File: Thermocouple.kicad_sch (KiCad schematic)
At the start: 9 parts, among them J7 K-TYPE THERMOCOUPLE, U7 MAX31856

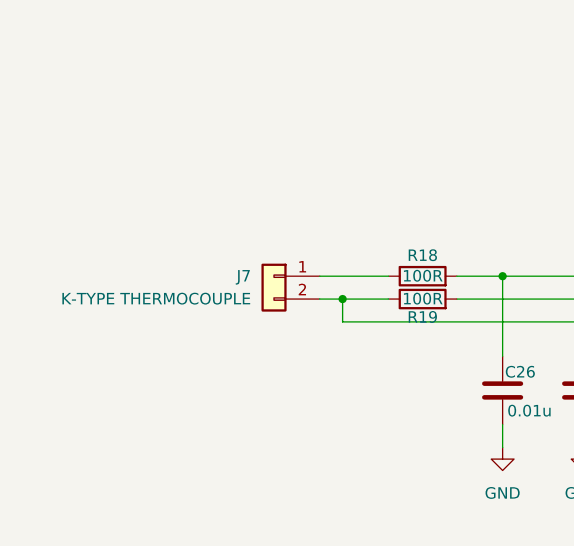
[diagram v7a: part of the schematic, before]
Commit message: Add screw terminals
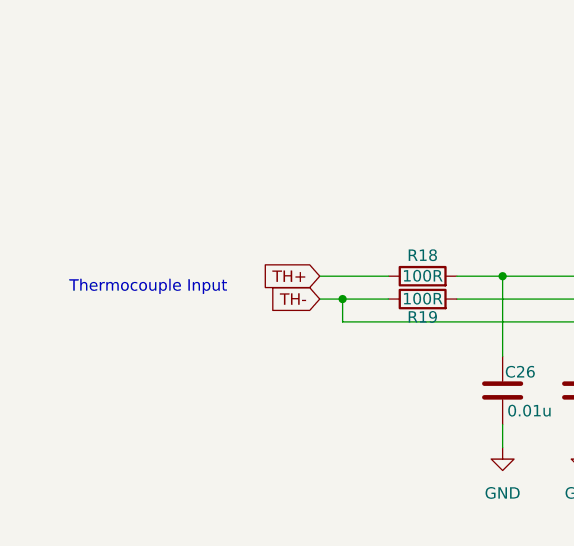
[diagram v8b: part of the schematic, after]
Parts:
- removed J7: K-TYPE THERMOCOUPLE, symbol Connector_Generic:Conn_01x02
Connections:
- net TH-: now reaches R19.1, U7.2 (BIAS)
- net TH+: now reaches R18.1
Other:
- note added: "Thermocouple Input"
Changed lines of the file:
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@@
 		(comment 1 "Customer: ESET")
+	)
+	(text "Thermocouple Input"
+		(exclude_from_sim no)
+		(at 87.63 87.63 0)
+		(effects
+			(font
+				(size 1.27 1.27)
+			)
+		)
 	)
 	(junction
@@
 				)
 				(justify left)
+			)
+		)
+	)
+	(global_label "TH-"
+		(shape input)
+		(at 106.68 88.9 180)
+		(fields_autoplaced yes)
+		(effects
+			(font
+				(size 1.27 1.27)
+			)
+			(justify right)
+		)
+		(property "Intersheetrefs" "${INTERSHEET_REFS}"
+			(at 99.8243 88.9 0)
+			(hide yes)
+			(show_name no)
+			(do_not_autoplace no)
+			(effects
+				(font
+					(size 1.27 1.27)
+				)
+				(justify right)
+			)
+		)
+	)
+	(global_label "TH+"
+		(shape input)
+		(at 106.68 86.36 180)
+		(fields_autoplaced yes)
+		(effects
+			(font
+				(size 1.27 1.27)
+			)
+			(justify right)
+		)
+		(property "Intersheetrefs" "${INTERSHEET_REFS}"
+			(at 99.8243 86.36 0)
+			(hide yes)
+			(show_name no)
+			(do_not_autoplace no)
+			(effects
+				(font
+					(size 1.27 1.27)
+				)
+				(justify right)
 			)
 		)
@@
 		(dnp no)
 		(fields_autoplaced yes)
-		(property "Reference" "#PWR054"
+		(property "Reference" "#PWR056"
 			(at 156.21 73.66 0)
 			(hide yes)
@@
 			(project "slapdaq-board"
 				(path "/13b31ec5-9d44-45c3-b3e5-a18c48e5f516/eb21b777-61c4-4e0c-995e-92861c8d5ad5"
-					(reference "#PWR054")
+					(reference "#PWR056")
 					(unit 1)
 				)
@@
 		(dnp no)
 		(fields_autoplaced yes)
-		(property "Reference" "#PWR053"
+		(property "Reference" "#PWR055"
 			(at 135.89 111.76 0)
 			(hide yes)
@@
 			(project "slapdaq-board"
 				(path "/13b31ec5-9d44-45c3-b3e5-a18c48e5f516/eb21b777-61c4-4e0c-995e-92861c8d5ad5"
-					(reference "#PWR053")
+					(reference "#PWR055")
 					(unit 1)
 				)
@@
 		(dnp no)
 		(fields_autoplaced yes)
-		(property "Reference" "#PWR052"
+		(property "Reference" "#PWR054"
 			(at 127 111.76 0)
 			(hide yes)
@@
 			(project "slapdaq-board"
 				(path "/13b31ec5-9d44-45c3-b3e5-a18c48e5f516/eb21b777-61c4-4e0c-995e-92861c8d5ad5"
-					(reference "#PWR052")
+					(reference "#PWR054")
 					(unit 1)
 				)
@@
 		(dnp no)
 		(fields_autoplaced yes)
-		(property "Reference" "#PWR057"
+		(property "Reference" "#PWR059"
 			(at 175.26 73.66 0)
 			(hide yes)
@@
 			(project "slapdaq-board"
 				(path "/13b31ec5-9d44-45c3-b3e5-a18c48e5f516/eb21b777-61c4-4e0c-995e-92861c8d5ad5"
-					(reference "#PWR057")
+					(reference "#PWR059")
 					(unit 1)
 				)
@@
 		(dnp no)
 		(fields_autoplaced yes)
-		(property "Reference" "#PWR056"
+		(property "Reference" "#PWR058"
 			(at 165.1 114.3 0)
 			(hide yes)
@@
 			(project "slapdaq-board"
 				(path "/13b31ec5-9d44-45c3-b3e5-a18c48e5f516/eb21b777-61c4-4e0c-995e-92861c8d5ad5"
-					(reference "#PWR056")
+					(reference "#PWR058")
 					(unit 1)
 				)
@@
 	)
 	(symbol
-		(lib_id "Connector_Generic:Conn_01x02")
-		(at 101.6 86.36 0)
-		(mirror y)
-		(unit 1)
-		(body_style 1)
-		(exclude_from_sim no)
-		(in_bom yes)
-		(on_board yes)
-		(in_pos_files yes)
-		(dnp no)
-		(fields_autoplaced yes)
-		(property "Reference" "J7"
-			(at 99.06 86.3599 0)
-			(show_name no)
-			(do_not_autoplace no)
-			(effects
-				(font
-					(size 1.27 1.27)
-				)
-				(justify left)
-			)
-		)
-		(property "Value" "K-TYPE THERMOCOUPLE"
-			(at 99.06 88.8999 0)
-			(show_name no)
-			(do_not_autoplace no)
-			(effects
-				(font
-					(size 1.27 1.27)
-				)
-				(justify left)
-			)
-		)
-		(property "Footprint" ""
-			(at 101.6 86.36 0)
-			(hide yes)
-			(show_name no)
-			(do_not_autoplace no)
-			(effects
-				(font
-					(size 1.27 1.27)
-				)
-			)
-		)
-		(property "Datasheet" ""
-			(at 101.6 86.36 0)
-			(hide yes)
-			(show_name no)
-			(do_not_autoplace no)
-			(effects
-				(font
-					(size 1.27 1.27)
-				)
-			)
-		)
-		(property "Description" "Generic connector, single row, 01x02, script generated (kicad-library-utils/schlib/autogen/connector/)"
-			(at 101.6 86.36 0)
-			(hide yes)
-			(show_name no)
-			(do_not_autoplace no)
-			(effects
-				(font
-					(size 1.27 1.27)
-				)
-			)
-		)
-		(property "Manufacturer" "Phoenix Contact"
-			(at 101.6 86.36 0)
-			(hide yes)
-			(show_name no)
-			(do_not_autoplace no)
-			(effects
-				(font
-					(size 1.27 1.27)
-				)
-			)
-		)
-		(property "MPN" ""
-			(at 101.6 86.36 0)
-			(hide yes)
-			(show_name no)
-			(do_not_autoplace no)
-			(effects
-				(font
-					(size 1.27 1.27)
-				)
-			)
-		)
-		(property "Mouser Link" ""
-			(at 101.6 86.36 0)
-			(hide yes)
-			(show_name no)
-			(do_not_autoplace no)
-			(effects
-				(font
-					(size 1.27 1.27)
-				)
-			)
-		)
-		(pin "1"
-		)
-		(pin "2"
-		)
-		(instances
-			(project "slapdaq-board"
-				(path "/13b31ec5-9d44-45c3-b3e5-a18c48e5f516/eb21b777-61c4-4e0c-995e-92861c8d5ad5"
-					(reference "J7")
-					(unit 1)
-				)
-			)
-		)
-	)
-	(symbol
 		(lib_id "power:+3.3V")
 		(at 165.1 54.61 0)
@@
 		(dnp no)
 		(fields_autoplaced yes)
-		(property "Reference" "#PWR055"
+		(property "Reference" "#PWR057"
 			(at 165.1 58.42 0)
 			(hide yes)
@@
 			(project "slapdaq-board"
 				(path "/13b31ec5-9d44-45c3-b3e5-a18c48e5f516/eb21b777-61c4-4e0c-995e-92861c8d5ad5"
-					(reference "#PWR055")
+					(reference "#PWR057")
 					(unit 1)
 				)
